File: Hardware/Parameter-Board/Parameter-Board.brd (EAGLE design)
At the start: 100 x 80 mm, 22 parts

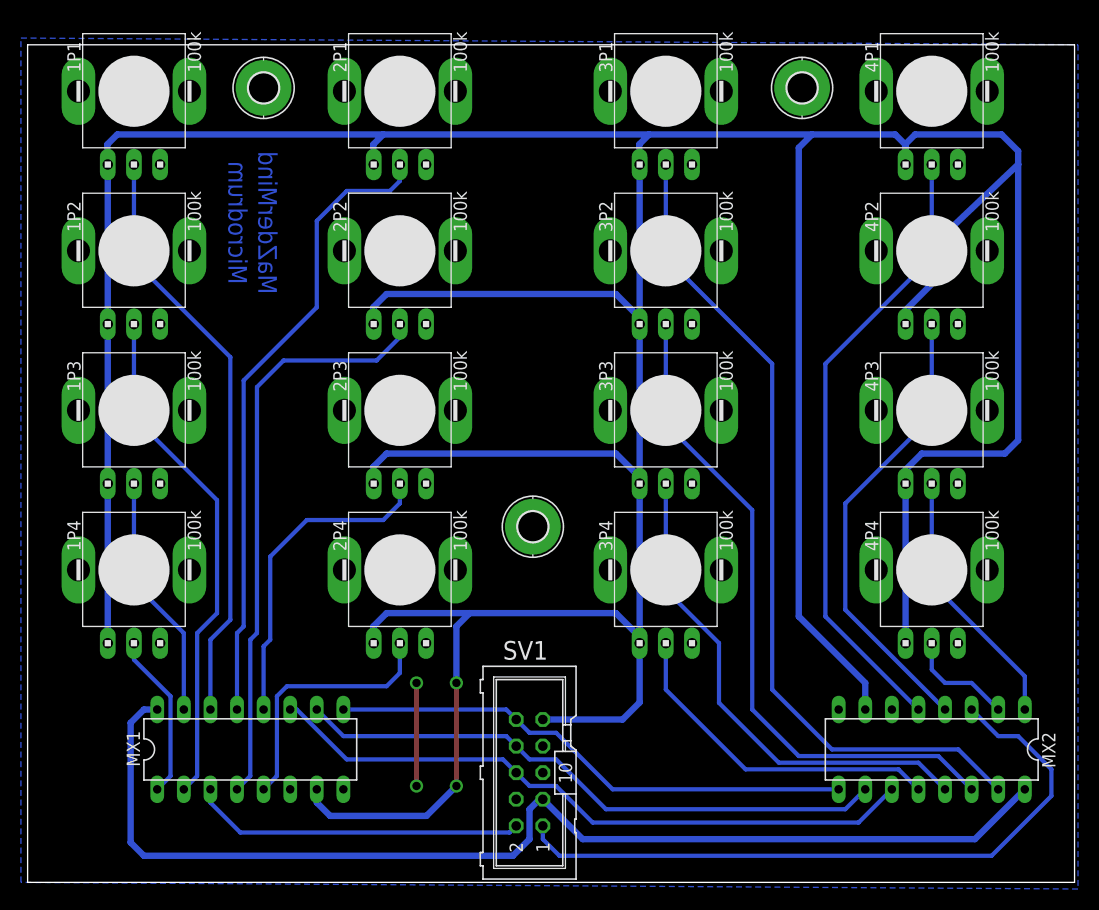
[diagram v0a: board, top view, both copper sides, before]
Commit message: VEE ist die negative Referenzspannung, welche in unserem Fall GND ist. Die Referenz-Voltage des MCU ist hingegen mit AGND verbunden.
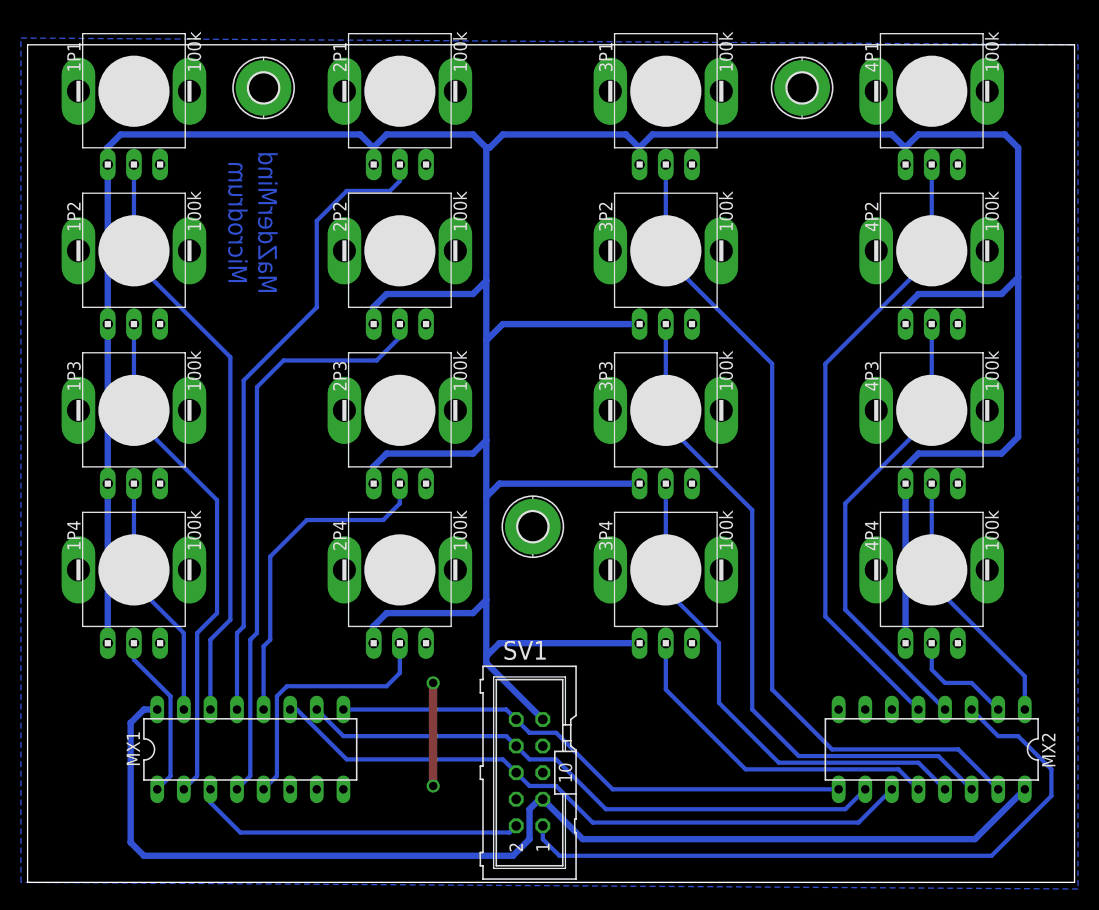
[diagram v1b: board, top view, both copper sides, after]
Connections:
- removed net VEE: 1P1.A, 1P2.A, 1P3.A, 1P4.A, 2P1.A, 2P2.A, 2P3.A, 2P4.A, 3P1.A, 3P2.A, 3P3.A, 3P4.A, 4P1.A, 4P2.A, 4P3.A, 4P4.A, MX1.7, MX2.7, SV1.9
- new net AGND: 1P1.A, 1P2.A, 1P3.A, 1P4.A, 2P1.A, 2P2.A, 2P3.A, 2P4.A, 3P1.A, 3P2.A, 3P3.A, 3P4.A, 4P1.A, 4P2.A, 4P3.A, 4P4.A, SV1.9
- net GND: now also MX1.7, MX2.7
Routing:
- net VEE: track 463.0 -> 0.00 mm, vias 2 -> 0
- net AGND: track 0.00 -> 359.0 mm

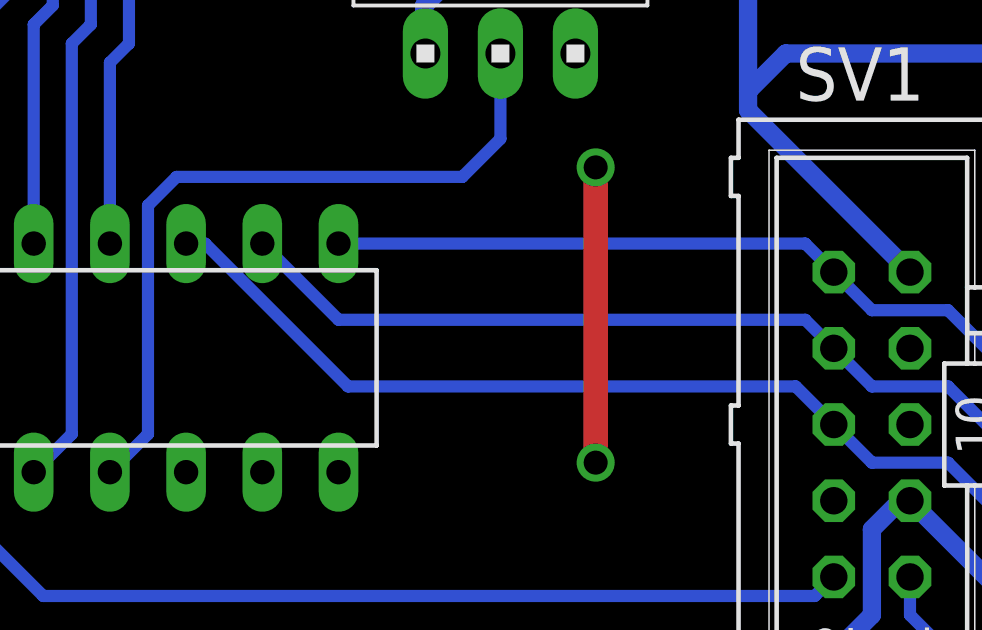
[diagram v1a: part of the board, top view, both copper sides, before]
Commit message: fix clearance problem
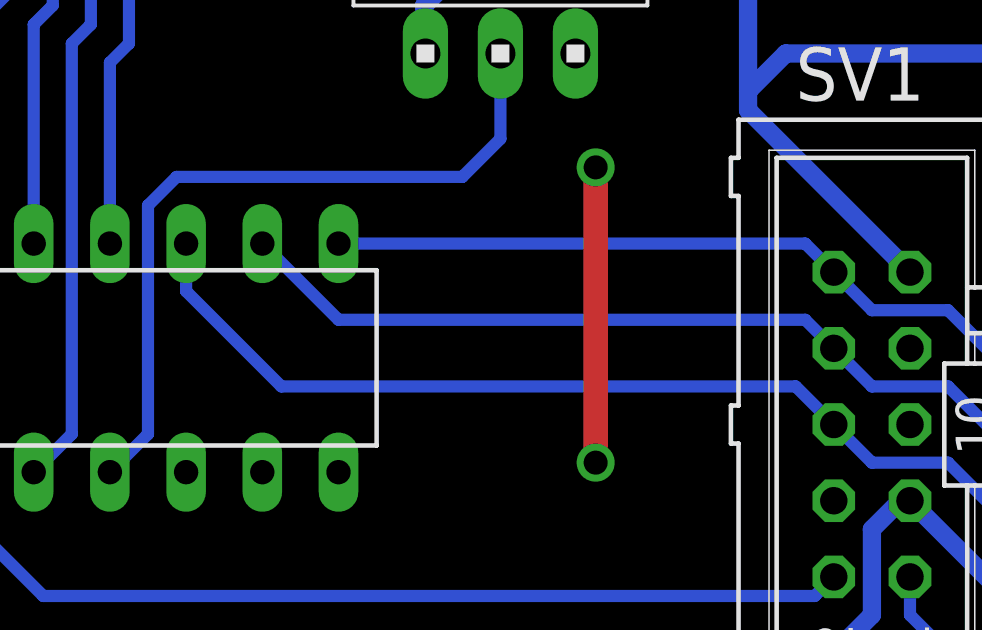
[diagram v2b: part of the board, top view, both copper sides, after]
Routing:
- net A: track 63.3 -> 64.2 mm
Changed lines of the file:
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@@
 <wire x1="50.4825" y1="9.2075" x2="47.9425" y2="9.2075" width="0.4064" layer="16"/>
 <wire x1="47.9425" y1="9.2075" x2="46.6725" y2="10.4775" width="0.4064" layer="16"/>
-<wire x1="25.0825" y1="16.51" x2="25.7175" y2="16.51" width="0.4064" layer="16"/>
-<wire x1="25.7175" y1="16.51" x2="30.48" y2="11.7475" width="0.4064" layer="16"/>
-<wire x1="30.48" y1="11.7475" x2="45.4025" y2="11.7475" width="0.4064" layer="16"/>
+<wire x1="25.0825" y1="16.51" x2="25.0825" y2="14.9225" width="0.4064" layer="16"/>
+<wire x1="25.0825" y1="14.9225" x2="28.2575" y2="11.7475" width="0.4064" layer="16"/>
+<wire x1="28.2575" y1="11.7475" x2="45.4025" y2="11.7475" width="0.4064" layer="16"/>
 <wire x1="45.4025" y1="11.7475" x2="46.6725" y2="10.4775" width="0.4064" layer="16"/>
 </signal>

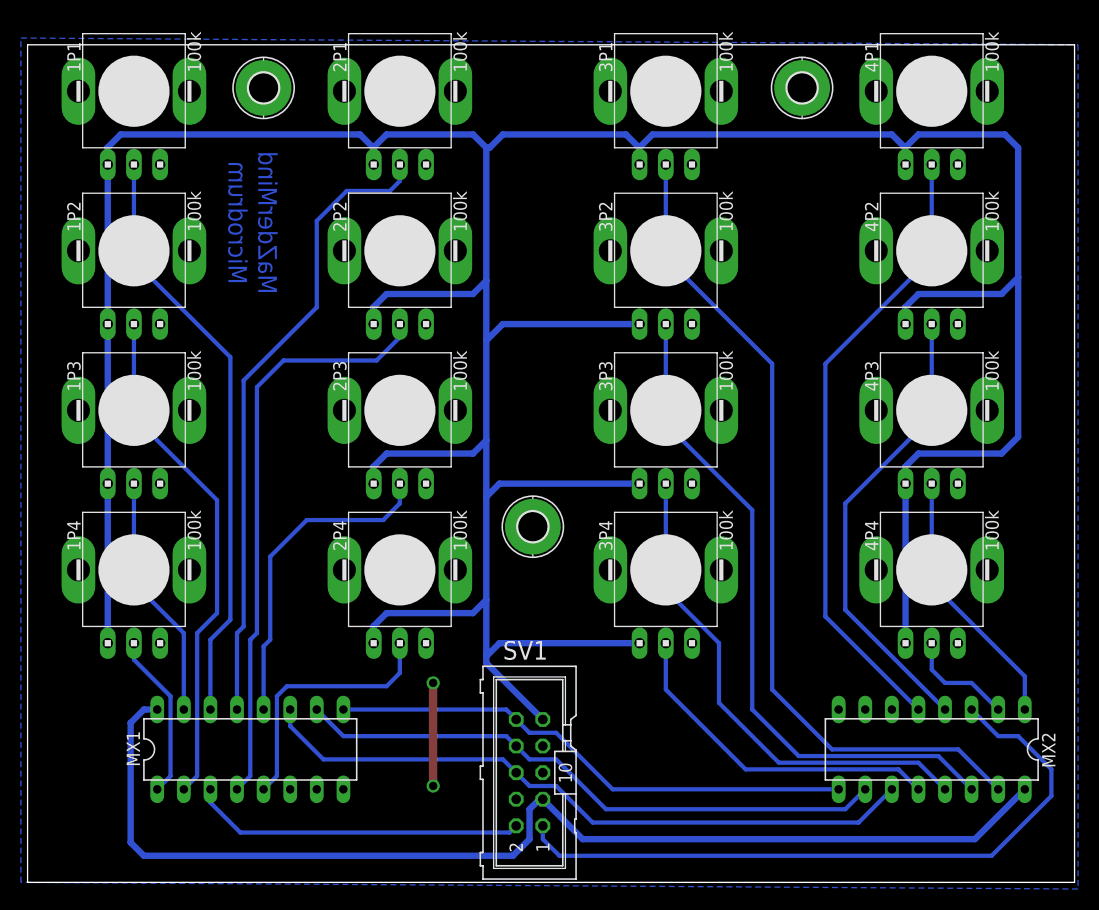
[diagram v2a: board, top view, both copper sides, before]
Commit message: Das komplette Board wurde neu geroutet, so dass keine Top-Layer-Brücke nötig und die Leiterbahnführung einheitlicher ist
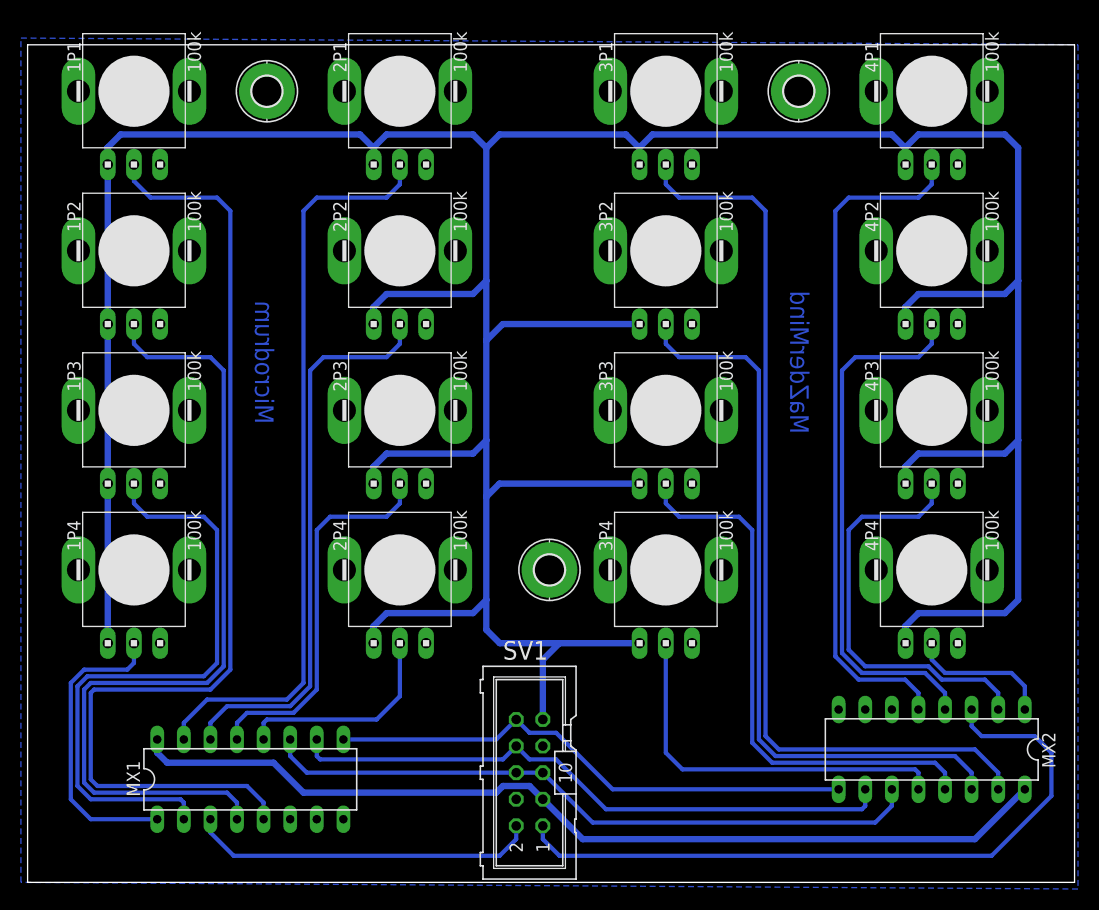
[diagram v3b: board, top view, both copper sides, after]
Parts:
- moved H1 4.42 mm to (49.8, 29.8)
- moved MX1 2.86 mm to (21.3, 9.84)
- moved H3 0.45 mm to (73.7, 75.6)
- moved H2 0.45 mm to (22.9, 75.6)
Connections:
- net 1P1: now also MX1.5; no longer MX1.14
- net 1P2: now also MX1.4; no longer MX1.2
- net 1P3: now also MX1.2; no longer MX1.15
- net 2P1: now also MX1.15; no longer MX1.13
- net 2P2: now also MX1.14; no longer MX1.4
- net 2P3: now also MX1.13; no longer MX1.12
- net 2P4: now also MX1.12; no longer MX1.5
- net 4P3: now also MX2.2; no longer MX2.1
- net 4P4: now also MX2.1; no longer MX2.2
- net A: now also SV1.5
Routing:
- net 1P1: track 56.7 -> 97.3 mm
- net 1P3: track 23.5 -> 59.8 mm
- net 1P2: track 49.0 -> 79.9 mm
- net VCC: track 107.9 -> 90.1 mm
- net 4P3: track 25.3 -> 39.9 mm
- net 1P4: track 15.9 -> 28.9 mm
- net 2P1: track 60.9 -> 71.8 mm
- net AGND: track 359.0 -> 369.6 mm
- net GND: track 9.84 -> 0.00 mm, vias 2 -> 0
- net 3P1: track 79.9 -> 87.9 mm
- net 4P2: track 44.2 -> 51.5 mm
- net 3P2: track 64.3 -> 70.3 mm
- net 4P1: track 59.9 -> 65.7 mm
- net 2P3: track 31.2 -> 36.6 mm
- net 3P3: track 48.1 -> 52.7 mm
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
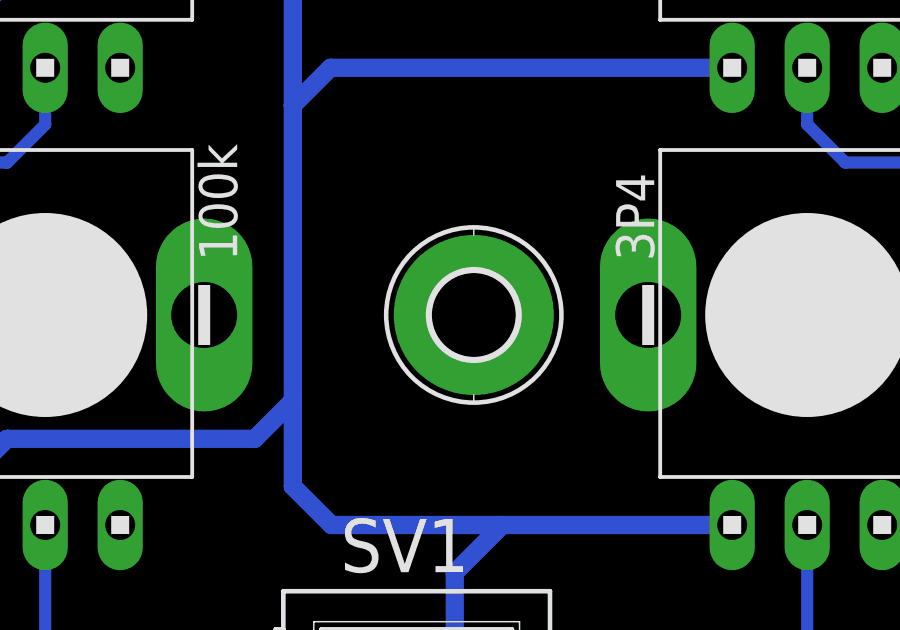
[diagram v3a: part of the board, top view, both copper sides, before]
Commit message: Das Mounthole wurde zwischen den Potentiometern zentriert
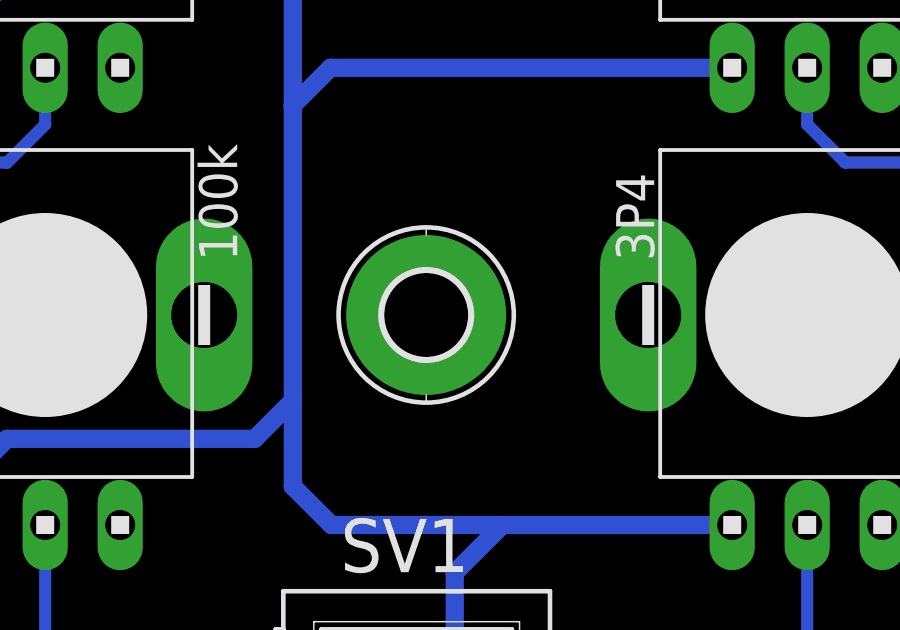
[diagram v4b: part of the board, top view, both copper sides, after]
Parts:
- moved H1 1.59 mm to (48.3, 29.8)
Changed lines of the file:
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@@
 <element name="2P2" library="alps" package="RK09K113" value="100k" x="35.56" y="60.325"/>
 <element name="2P1" library="alps" package="RK09K113" value="100k" x="35.56" y="75.565"/>
-<element name="H1" library="holes" package="2,8-PAD" value="MOUNT-PAD-ROUND2.8" x="49.8475" y="29.845"/>
+<element name="H1" library="holes" package="2,8-PAD" value="MOUNT-PAD-ROUND2.8" x="48.26" y="29.845"/>
 <element name="H2" library="holes" package="2,8-PAD" value="MOUNT-PAD-ROUND2.8" x="22.86" y="75.565"/>
 <element name="H3" library="holes" package="2,8-PAD" value="MOUNT-PAD-ROUND2.8" x="73.66" y="75.565"/>

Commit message: Endgültiges Boardlayout
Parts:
- H1, H2, H3: value MOUNT-PAD-ROUND2.8 -> MOUNT-PAD-ROUND3.2; device holes:2,8-PAD -> holes:3,2-PAD
- moved H2 101.0 mm to (95.2, 5.08)
- moved H1 49.8 mm to (5.08, 5.08)
- moved H3 24.1 mm to (49.5, 75.6)
- moved MX2 11.5 mm to (74.9, 14.0), turned to 270 degrees
- moved MX1 5.02 mm to (24.1, 14.0), turned to 270 degrees
- moved SV1 1.62 mm to (49.5, 10.2), turned to 270 degrees
- moved 1P2 1.42 mm to (11.4, 59.7)
- moved 1P3 1.42 mm to (11.4, 44.5)
- moved 1P4 1.42 mm to (11.4, 29.2)
- moved 2P2 1.42 mm to (36.8, 59.7)
- moved 3P2 1.42 mm to (62.2, 59.7)
- moved 4P2 1.42 mm to (87.6, 59.7)
- moved 2P3 1.42 mm to (36.8, 44.5)
- moved 2P4 1.42 mm to (36.8, 29.2)
- moved 3P3 1.42 mm to (62.2, 44.5)
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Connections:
- net 1P2 renamed 7MX1
- removed net 1P1: 1P1.C, MX1.5
- removed net 1P3: 1P3.C, MX1.2
- removed net 1P4: 1P4.C, MX1.1
- removed net 2P1: 2P1.C, MX1.15
- removed net 2P2: 2P2.C, MX1.14
- removed net 2P3: 2P3.C, MX1.13
- removed net 2P4: 2P4.C, MX1.12
- removed net 3P1: 3P1.C, MX2.15
- removed net 3P2: 3P2.C, MX2.14
- removed net 3P3: 3P3.C, MX2.13
- removed net 3P4: 3P4.C, MX2.12
- removed net 4P1: 4P1.C, MX2.5
- removed net 4P2: 4P2.C, MX2.4
- removed net 4P3: 4P3.C, MX2.2
- removed net 4P4: 4P4.C, MX2.1
- new net 0MX1: 2P4.C, MX1.13
- new net 0MX2: 4P3.C, MX2.13
- new net 1MX1: 2P3.C, MX1.14
- new net 1MX2: 4P2.C, MX2.14
- new net 2MX1: 2P2.C, MX1.15
- new net 2MX2: 4P1.C, MX2.15
- new net 3MX1: 1P4.C, MX1.12
- new net 3MX2: 4P4.C, MX2.12
- new net 4MX1: 1P1.C, MX1.1
- new net 4MX2: 3P1.C, MX2.1
- new net 5MX1: 1P3.C, MX1.5
- new net 5MX2: 3P4.C, MX2.5
- new net 6MX1: 2P1.C, MX1.2
- new net 6MX2: 3P2.C, MX2.2
- new net 7MX2: 3P3.C, MX2.4
- net A: no longer SV1.5
- net AGND: now also 2P1.B, 2P2.B, 2P3.B, 2P4.B, 4P1.B, 4P2.B, 4P3.B, 4P4.B, SV1.4; no longer 2P1.A, 2P2.A, 2P3.A, 2P4.A, 4P1.A, 4P2.A, 4P3.A, 4P4.A, SV1.9
- net GND: now also 2P1.A, 2P2.A, 2P3.A, 2P4.A, 4P1.A, 4P2.A, 4P3.A, 4P4.A, SV1.2; no longer 2P1.B, 2P2.B, 2P3.B, 2P4.B, 4P1.B, 4P2.B, 4P3.B, 4P4.B, SV1.4
- net VCC: now also SV1.1; no longer SV1.3
- net X1: now also SV1.3; no longer SV1.2
- net X2: now also SV1.5; no longer SV1.1
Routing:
- net 1P1: track 97.3 -> 0.00 mm
- net 3P1: track 87.9 -> 0.00 mm
- net 2P1: track 71.8 -> 0.00 mm
- net 3P2: track 70.3 -> 0.00 mm
- net 4P1: track 65.7 -> 0.00 mm
- net AGND: track 369.6 -> 305.5 mm
- net 6MX1: track 0.00 -> 64.1 mm
- net 2MX2: track 0.00 -> 62.9 mm
- net 1P3: track 59.8 -> 0.00 mm
- net GND: track 0.00 -> 59.7 mm, vias 0 -> 2
- net 4MX2: track 0.00 -> 56.5 mm
- net 4MX1: track 0.00 -> 56.5 mm
- net 2P2: track 54.2 -> 0.00 mm
- net 3P3: track 52.7 -> 0.00 mm
- net 4P2: track 51.5 -> 0.00 mm
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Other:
- board text added: "by MaZderMind"
- board text removed: "MaZderMind"
